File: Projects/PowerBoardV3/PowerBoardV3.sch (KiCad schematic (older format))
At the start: 30 parts

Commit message: Powerboard V3, Notes in the logbook
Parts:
- added C? (x2): 1 uF, symbol C_Small
- added C? (x2): 10 uF, symbol C_Small
- added Q?: 2N3904, TO_SOT_Packages_THT:TO-92_Molded_Narrow, symbol 2N3904
- added Q?: 2N3906, TO_SOT_Packages_THT:TO-92_Molded_Narrow, symbol 2N3906
- added R? (x2): 100, symbol R_Small
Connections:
- net A: now also R?.2
- net BAT: now also C?.1, R?.2
- net BOOT_TS1: now also Q?.3 (C); no longer U?.4 (PA03)
- net BOOT_VC1: now also Q?.1 (E); no longer U?.3 (PA02)
- net GND: now also C?.1, C?.2, C?.2
- net VC5x: now also C?.1, C?.2, Q?.2 (B), R?.1
- net at C?.1, C?.2, R?.2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: now also U?.23 (VC4)
- net at U?.7 (CAP1): now also C?.2
- net REGSRC: now reaches U?.9 (REGSRC)
- net REGSRC: now also C?.1, Q?.1 (E)
- new net: Q?.3 (C), R?.1
- new net Micrcontroller: Q?.2 (B)
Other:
- note removed: "Can analog pins physically connect using input from controller code?"

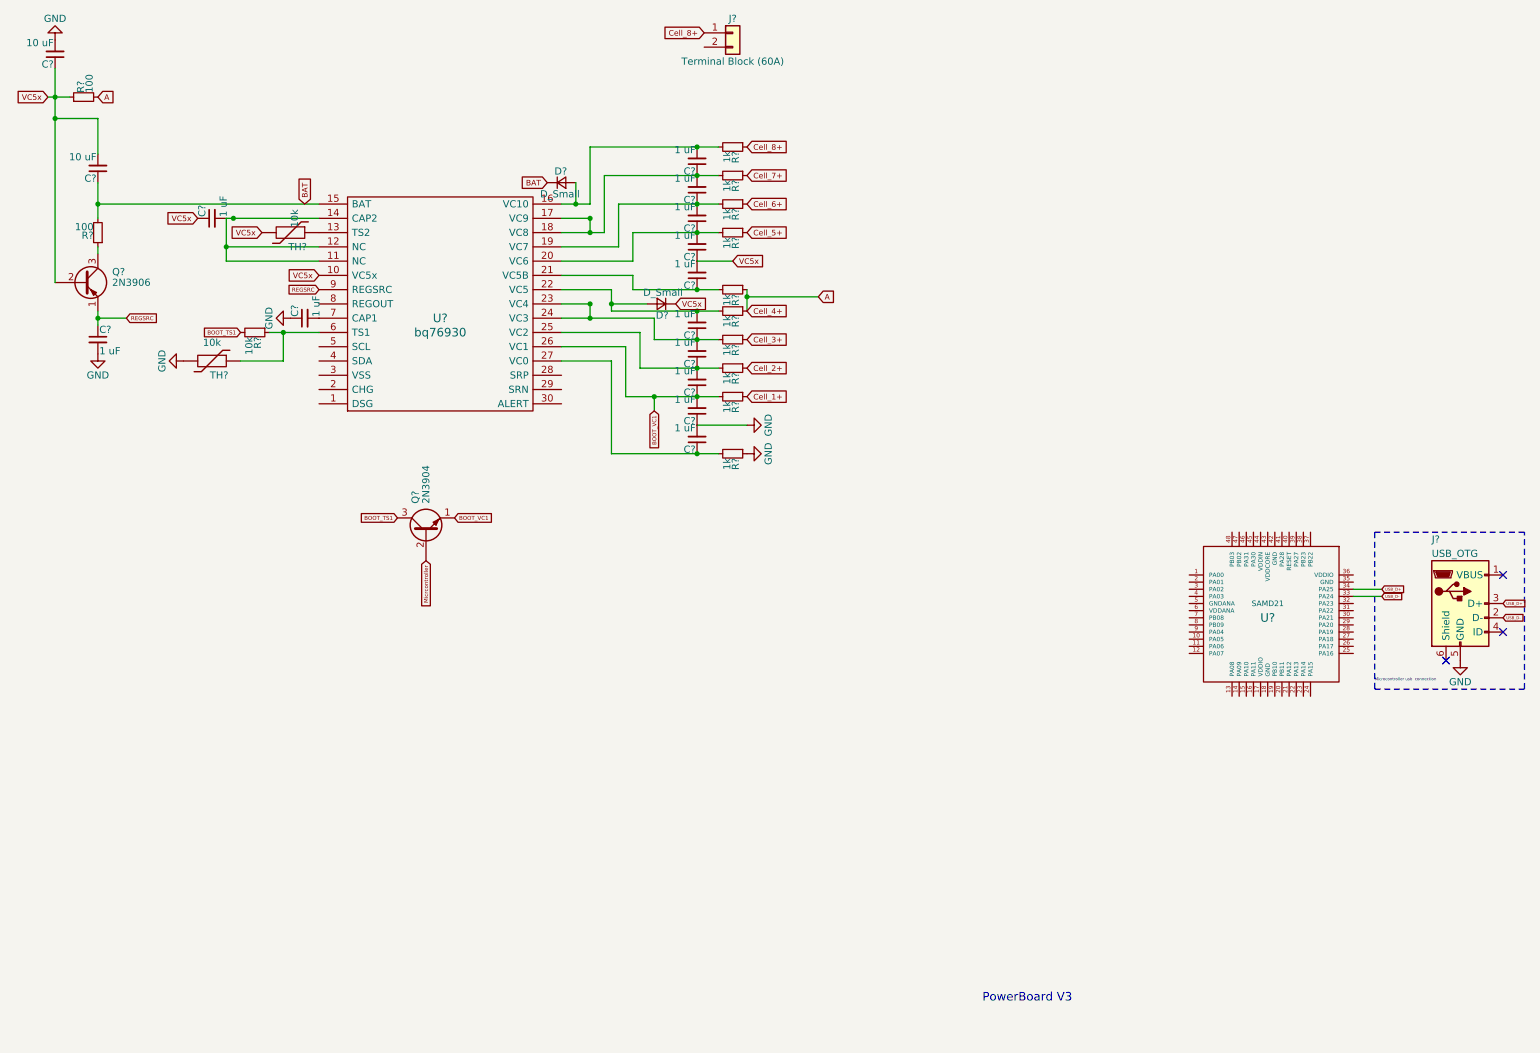
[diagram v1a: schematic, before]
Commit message: Hierarchy Schematic
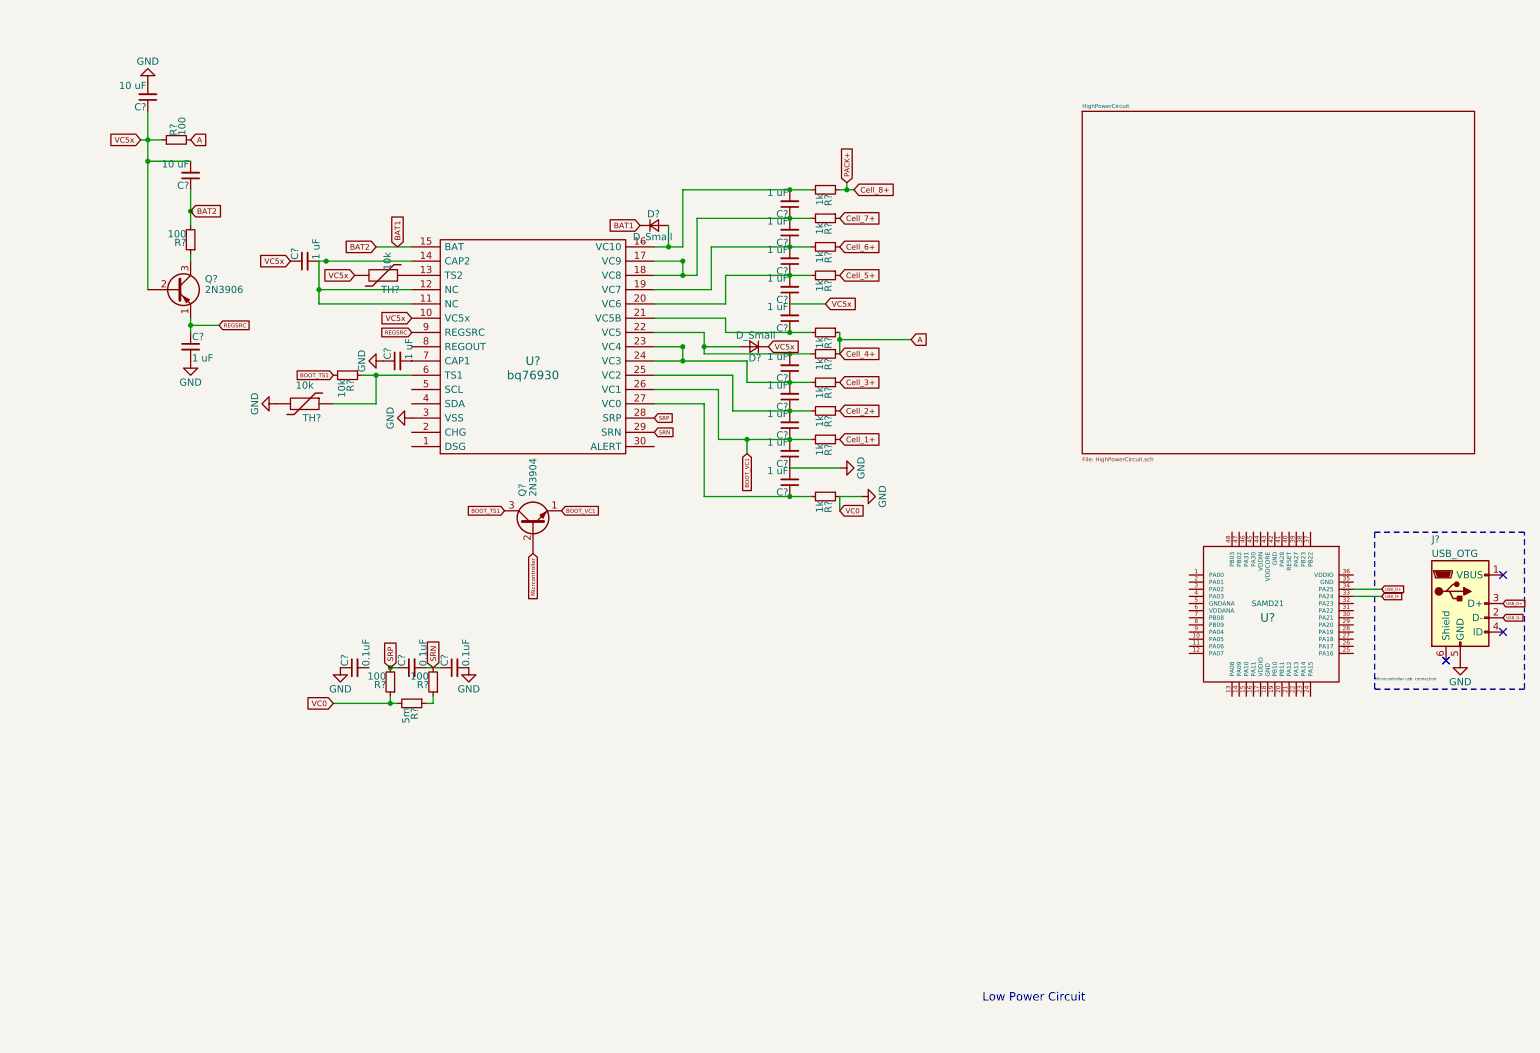
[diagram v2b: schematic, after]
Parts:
- removed J?: Terminal Block (60A), symbol Conn_01x02
- added C? (x3): 0.1uF, symbol C_Small
- added R? (x2): 100, symbol R_Small
- added R?: 5m, symbol R_Small
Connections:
- net GND: now also U?.3 (VSS), C?.1, C?.2, R?.1, R?.2
- net SRP: now reaches U?.28 (SRP)
- net SRP: now also C?.1, R?.2
- net SRN: now reaches U?.29 (SRN)
- net SRN: now also C?.1, C?.2, R?.2
- net BAT renamed BAT1
- new net: R?.1, R?.1
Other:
- note added: "Low Power Circuit\n"
- note removed: "PowerBoard V3"
- moved on the sheet: C?, D?, Q?, R?, TH?, U?

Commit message: Clean Up of Schematic
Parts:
- removed C? (x13): 1 uF, symbol C_Small
- removed C? (x2): 10 uF, symbol C_Small
- removed C? (x3): 0.1uF, symbol C_Small
- removed D? (x2): D_Small, symbol D_Small
- removed J?: USB_OTG, symbol USB_OTG
- removed Q?: 2N3904, TO_SOT_Packages_THT:TO-92_Molded_Narrow, symbol 2N3904
- removed Q?: 2N3906, TO_SOT_Packages_THT:TO-92_Molded_Narrow, symbol 2N3906
- removed R? (x10): 1k, symbol R_Small
- removed R?: 10k, symbol R_Small
- removed R? (x4): 100, symbol R_Small
- removed R?: 5m, symbol R_Small
- removed TH? (x2): 10k, symbol Thermistor
- removed U?: SAMD21, symbol SAMD21
- removed U?: bq76930, symbol bq76930
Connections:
- no-connect marks 3 -> 0
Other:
- note removed: "Microcontroller usb connection"

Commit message: Worked on LPC, More infor in Log
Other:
- note added: "Blackbox\n\n"
- note added: "Is there supposed to be a diode parallel to the BSS84 transistor\n in the PTC circuit. (Refer to bq Datasheet)?"
- note removed: "Low Power Circuit\n"
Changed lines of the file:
@@
 Comment4 ""
 $EndDescr
-Text Notes 7350 7500 0    59   ~ 0
-Low Power Circuit\n
+Text Notes 7350 7600 0    59   ~ 0
+Blackbox\n\n
 $Sheet
 S 8050 1250 2750 2400
@@
 F1 "LowPowerCircuit.sch" 60
 $EndSheet
+Text Notes 8000 3850 0    39   ~ 0
+Is there supposed to be a diode parallel to the BSS84 transistor\n in the PTC circuit. (Refer to bq Datasheet)?
 $EndSCHEMATC
